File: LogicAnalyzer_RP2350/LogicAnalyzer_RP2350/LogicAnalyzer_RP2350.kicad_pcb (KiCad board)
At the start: 4 copper layers, 100 x 80 mm, 152 parts, among them J1 USB_C_Receptacle_USB2.0_16P, J2 SM03B-SRSS-TB, J3 SSW-106-02-TM-S-RA, J4 534269030, J5 534269030, J6 612050235221, J7 533984003, J8 2035571207, SW1 SW_MEC_5G, SW2 SW_MEC_5G, U1 NCP1117ST33T3G, U10 TXU0104PWR, U11 ATtiny3216-S, U2 TPS2552DRVR-1, U3 W25Q128JVS, U4 RP2350A, U5 TXU0104PWR, U6 TXU0104PWR, U7 TXU0104PWR, U8 TXU0104PWR, U9 TXU0104PWR, Y1 12Mhz

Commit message: Some PLacments
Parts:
- moved R3 6.99 mm to (133.8, 59.0), turned to 90 degrees
- moved L2 5.51 mm to (132.2, 67.3), turned to 180 degrees
- moved C3 4.51 mm to (125.9, 65.0)
- moved C2 4.35 mm to (131.3, 64.1)
- moved R33 3.93 mm to (145.0, 97.5)
- moved R34 3.93 mm to (146.0, 97.5)
- moved R35 3.93 mm to (147.0, 97.5)
- moved R14 3.42 mm to (140.7, 96.8)
- moved R4 3.18 mm to (146.5, 59.2), turned to 90 degrees
- moved R29 2.46 mm to (131.2, 97.5)
- moved R30 2.46 mm to (132.2, 97.5)
- moved R31 2.46 mm to (133.2, 97.5)
- moved R32 2.46 mm to (134.2, 97.5)
- moved C1 2.41 mm to (133.3, 64.1), turned to 90 degrees
- moved Y1 1.93 mm to (138.5, 98.1)
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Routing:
- net +3.3V: track 0.00 -> 18.1 mm, vias 0 -> 7
- net /RP2350_Main/GP12: track 0.00 -> 8.83 mm
- net /RP2350_Main/GP13: track 0.00 -> 8.46 mm
- net /RP2350_Main/GP14: track 0.00 -> 7.97 mm
- net /RP2350_Main/GP15: track 0.00 -> 7.36 mm
- net /RP2350_Main/GP18: track 0.00 -> 6.72 mm
- net /RP2350_Main/GP17: track 0.00 -> 6.53 mm
- net /RP2350_Main/GP16: track 0.00 -> 5.76 mm
- net +1V1: track 0.00 -> 4.98 mm, vias 0 -> 2
- net /RP2350_Main/XOUT: track 7.14 -> 3.23 mm
- net Net-(U2-ILIM): track 3.72 -> 0.00 mm
- net GND: track 0.00 -> 3.31 mm, vias 0 -> 6
- net Net-(U2-EN): track 2.41 -> 0.08 mm
- net Net-(U2-*FAULT): track 2.31 -> 0.00 mm
- net Net-(C13-Pad1): track 2.70 -> 4.93 mm
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
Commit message: Routing for Micro Controller Section Done
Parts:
- added C3: 4.7uF, Capacitor_SMD:C_0805_2012Metric_Pad1.18x1.45mm_HandSolder, F.Cu at (118.5, 61.0)
- C10, C11: footprint Capacitor_SMD:C_0402_1005Metric_Pad0.74x0.62mm_HandSolder -> Capacitor_0402 Small Pads for RP2350 VREG:C_0402_1005Metric_small_pads
- L3: footprint ABRACON AOTA-B201610S3R3-101-T:AOTAB201610S3R3101T -> Inductor_RP2350_Foot Print:L_pol_2016
- moved C7 8.37 mm to (109.7, 63.6)
- moved C4 8.37 mm to (98.2, 75.9)
- moved C5 8.37 mm to (109.2, 70.1)
- moved C6 8.37 mm to (107.7, 75.9)
- moved R1 8.37 mm to (99.4, 66.1)
- moved R2 8.37 mm to (99.4, 67.6)
- moved R5 8.37 mm to (105.4, 66.6)
- moved R6 8.37 mm to (105.4, 68.1)
- moved R7 8.37 mm to (105.4, 65.1)
- moved U1 8.37 mm to (102.9, 75.6)
- moved U2 8.37 mm to (109.2, 67.4)
- moved C8 5.61 mm to (120.7, 72.1)
- moved C9 5.61 mm to (119.7, 72.1)
- moved R8 5.61 mm to (120.0, 79.4)
- moved R9 5.61 mm to (120.0, 77.6)
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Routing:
- net +3.3V: track 18.1 -> 57.4 mm, vias 7 -> 21
- net GND: track 3.31 -> 39.8 mm, vias 6 -> 47
- net /LevelShifters/D1: track 0.00 -> 30.5 mm
- net /LevelShifters/D2: track 0.00 -> 29.1 mm
- net /LevelShifters/D3: track 0.00 -> 27.9 mm
- net /LevelShifters/D24: track 0.00 -> 27.1 mm
- net /LevelShifters/D4: track 0.00 -> 26.4 mm
- net /LevelShifters/D23: track 0.00 -> 26.0 mm
- net /LevelShifters/D22: track 0.00 -> 24.9 mm
- net /LevelShifters/D21: track 0.00 -> 23.5 mm
- net /LevelShifters/D5: track 0.00 -> 20.3 mm
- net /RP2350_Main/QSPI_SS: track 0.00 -> 20.0 mm
- net /LevelShifters/D9: track 0.00 -> 19.3 mm
- net /LevelShifters/D6: track 0.00 -> 19.0 mm
- net /FrontPanelInterface/VREF: track 0.00 -> 19.0 mm, vias 0 -> 6
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- added copper zone on F.Cu, net +1V1
- added copper zone on F.Cu, net +3.3V
- added copper zone on F.Cu, net GND
- added copper zone on F.Cu, net Net-(U4-VREG_LX)

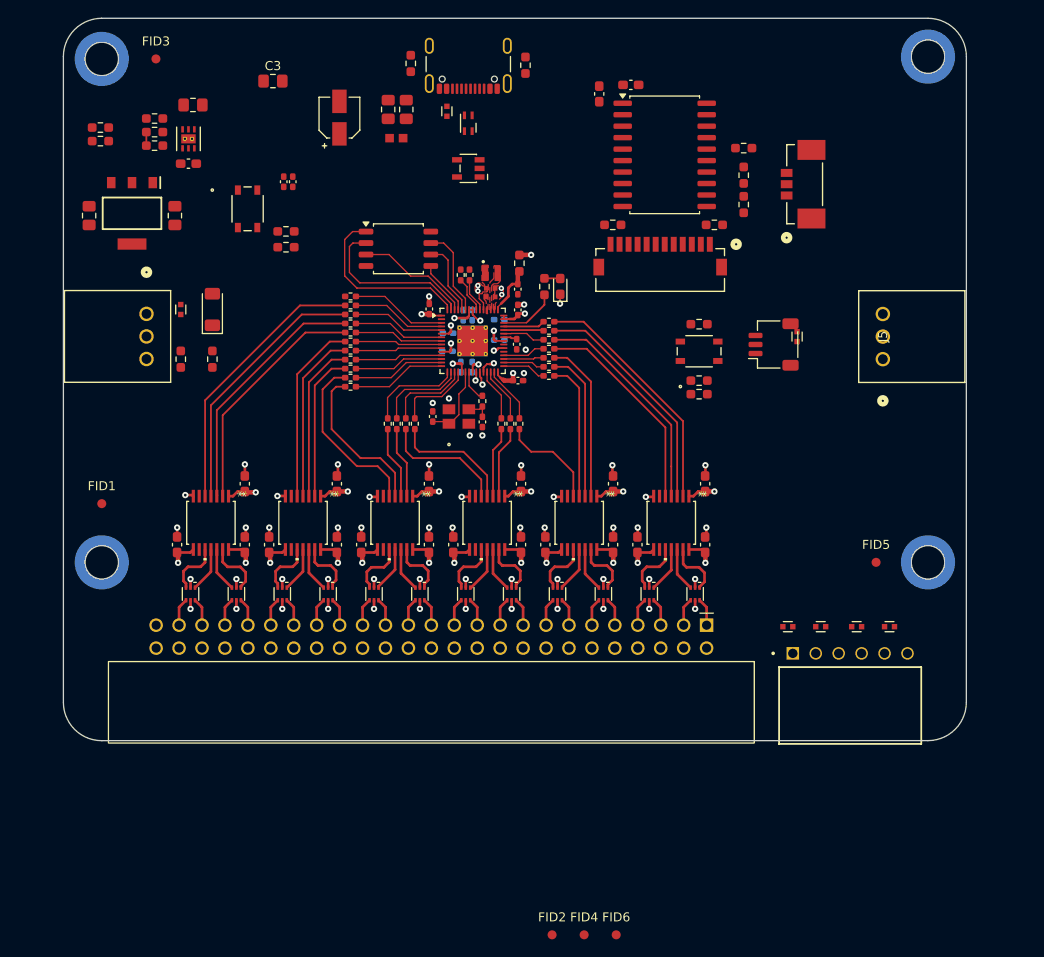
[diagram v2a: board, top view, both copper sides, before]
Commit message: Initial Routing Done, almost there
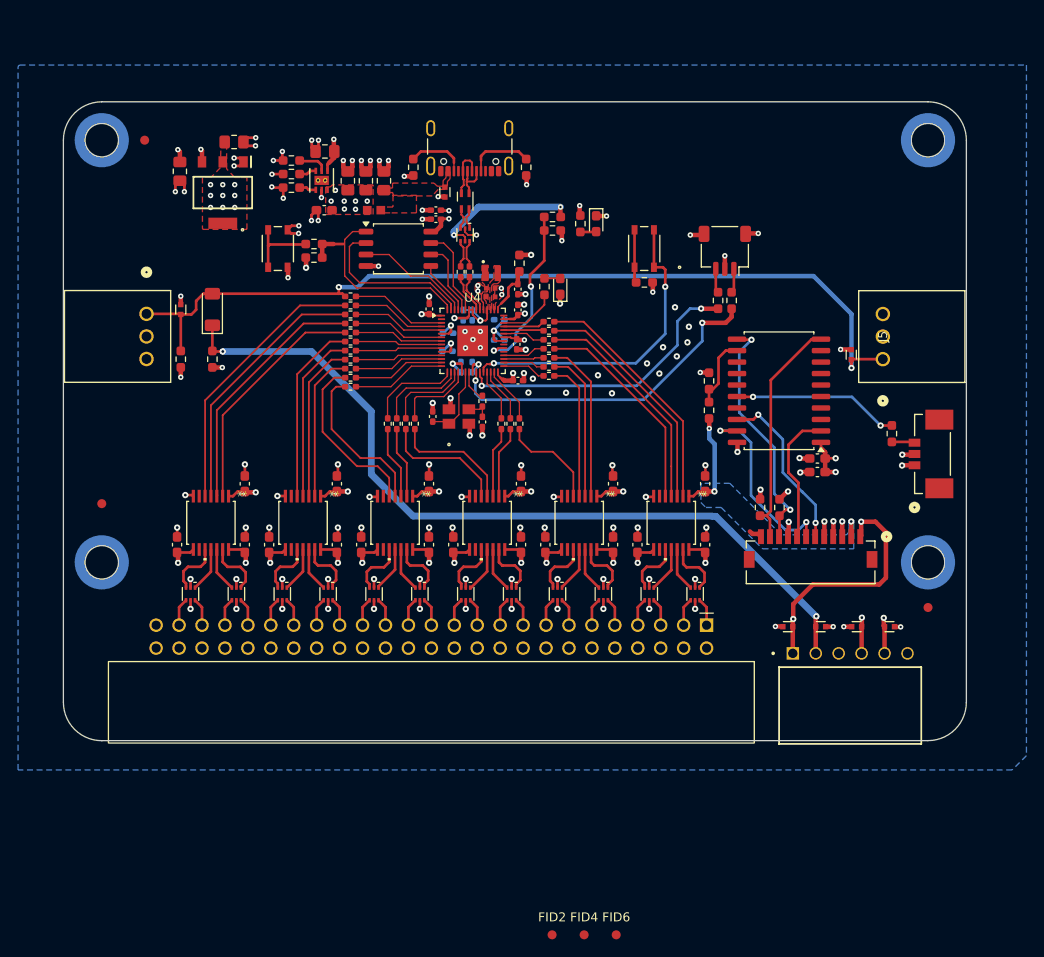
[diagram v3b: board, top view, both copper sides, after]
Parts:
- removed the C3 at (125.9, 65.0)
- added D23: LED_Blue, LED_SMD:LED_0603_1608Metric_Pad1.05x0.95mm_HandSolder, F.Cu at (154.3, 76.8)
- added R50: 470R, Resistor_SMD:R_0603_1608Metric_Pad0.98x0.95mm_HandSolder, F.Cu at (152.6, 76.8)
- D2: value SOT23-5L_824011 -> SOT563_82400152; footprint Diode_SMD_Wurth:D_Wurth_WE-TVS-SOT23-5L -> Diode_SMD_Wurth:D_Wurth_WE-TVS-SOT563
- U4: footprint Package_DFN_QFN:QFN-60-1EP_7x7mm_P0.4mm_EP3.4x3.4mm_ThermalVias -> Package_DFN_QFN:QFN-60-1EP_7x7mm_P0.4mm_EP3.4x3.4mm
- moved R1 51.0 mm to (149.5, 76.0)
- moved R2 51.0 mm to (149.5, 77.5)
- moved C46 48.3 mm to (178.8, 104.3), turned to 180 degrees
- moved C45 46.2 mm to (178.8, 102.8), turned to 180 degrees
- moved J8 36.4 mm to (178.1, 114.3)
- moved R47 35.6 mm to (187.1, 100.0), turned to 90 degrees
- moved R49 35.3 mm to (172.5, 108.2), turned to 90 degrees
- moved J7 33.1 mm to (191.6, 102.3)
- moved R48 32.1 mm to (174.6, 108.2), turned to 90 degrees
- moved U11 29.0 mm to (174.6, 95.3), turned to 180 degrees
- moved R45 26.3 mm to (166.8, 97.4), turned to -90 degrees
- moved R46 19.9 mm to (166.8, 94.2), turned to -90 degrees
- moved C9 17.1 mm to (136.6, 75.3), turned to 180 degrees
- moved C8 16.4 mm to (136.6, 76.3), turned to 180 degrees
- moved C5 15.9 mm to (124.2, 75.3)
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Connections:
- D2 pad 1: unconnected-(D2-NC-Pad1) -> /USB & POWER/TUSBC-
- D2 pad 3: /RP2350_Main/USB+ -> /USB & POWER/TUSBC+
- D2 pad 4: /RP2350_Main/USB- -> /RP2350_Main/USB+
- L1 pad 1: /USB & POWER/USBC+ -> /USB & POWER/TUSBC+
- L1 pad 2: /RP2350_Main/USB+ -> /USB & POWER/USBC+
- L1 pad 3: /RP2350_Main/USB- -> /USB & POWER/USBC-
- L1 pad 4: /USB & POWER/USBC- -> /USB & POWER/TUSBC-
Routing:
- net /LevelShifters/EXT_CHAIN: track 0.00 -> 97.9 mm, vias 0 -> 2
- net /LevelShifters/EXT_TRIG: track 0.00 -> 90.1 mm, vias 0 -> 2
- net GND: track 39.8 -> 110.0 mm, vias 47 -> 115
- net +3.3V: track 57.4 -> 93.9 mm, vias 21 -> 40
- net /RP2350_Main/SWCLK: track 1.01 -> 37.0 mm, vias 1 -> 2
- net Net-(U4-RUN): track 1.84 -> 34.8 mm, vias 1 -> 2
- net +5V: track 11.4 -> 43.4 mm, vias 12 -> 20
- net /RP2350_Main/SWDIO: track 1.85 -> 33.1 mm, vias 1 -> 2
- net Net-(U11-PB0): track 0.00 -> 27.2 mm, vias 0 -> 2
- net /FrontPanelInterface/EXTVREF: track 0.00 -> 26.9 mm, vias 0 -> 2
- net Net-(U11-PB1): track 0.00 -> 26.5 mm
- net /FrontPanelInterface/LEDB: track 0.00 -> 21.4 mm, vias 0 -> 2
- net /FrontPanelInterface/LEDA: track 0.00 -> 18.8 mm, vias 0 -> 2
- net Net-(U11-~{RESET}/PA0): track 0.00 -> 18.5 mm, vias 0 -> 2
- net /RP2350_Main/VBUS_SENSE: track 1.22 -> 19.3 mm, vias 1 -> 2
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- added copper zone on In2.Cu, net +1V1
- added copper zone on In2.Cu, net +3.3V
- added copper zone on In2.Cu, net +5V
- added copper zone on B.Cu, net /FrontPanelInterface/VREF
- added copper zone on In2.Cu, net /FrontPanelInterface/VREF
- added copper zone on F.Cu, net /USB & POWER/VBUS
- added copper zone on F.Cu, net /USB & POWER/VBUS_FILT
- added copper zone on In2.Cu, net /USB & POWER/VBUS_FILT
- added copper zone on B.Cu, net GND
- added copper zone on In1.Cu, net GND
- added copper zone on In2.Cu, net GND
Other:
- board size 100 x 80 mm -> 100 x 70.7 mm

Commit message: more routing
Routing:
- net /RP2350_Main/VBUS_SENSE: track 19.3 -> 26.1 mm
- net +3.3V: track 93.9 -> 90.8 mm
- net Net-(U11-PB1): track 26.5 -> 29.1 mm
- net /FrontPanelInterface/EXTVREF: track 26.9 -> 28.9 mm, vias 2 -> 0
- net GND: track 110.0 -> 109.3 mm, vias 115 -> 107
- added copper zone on B.Cu, net +3.3V
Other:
- rule pad_to_mask_clearance: 0.1 -> 0.035
- rule solder_mask_min_width: 0.1 -> 0.035

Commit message: Almost there
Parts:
- added REF**: KiCad-Logo2_5mm_SilkScreen, Symbol:KiCad-Logo2_5mm_SilkScreen, F.Cu at (103.7, 101.1)
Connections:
- net /RP2350_Main/USB_BOOT renamed /RP2350_Main/RP_BOOT
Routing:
- net GND: track 109.3 -> 107.8 mm, vias 107 -> 106

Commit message: Correcting Diff pair USB
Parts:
- moved D2 3.97 mm to (140.8, 74.2)
- moved L1 3.54 mm to (140.8, 77.7)
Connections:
- D2 pad 1: /USB & POWER/TUSBC- -> /USB & POWER/USBC-
- D2 pad 3: /USB & POWER/TUSBC+ -> /USB & POWER/USBC+
- D2 pad 4: /RP2350_Main/USB+ -> /USB & POWER/TUSBC+
- D2 pad 6: /RP2350_Main/USB- -> /USB & POWER/TUSBC-
- L1 pad 1: /USB & POWER/TUSBC+ -> /RP2350_Main/USB+
- L1 pad 2: /USB & POWER/USBC+ -> /USB & POWER/TUSBC+
- L1 pad 3: /USB & POWER/USBC- -> /USB & POWER/TUSBC-
- L1 pad 4: /USB & POWER/TUSBC- -> /RP2350_Main/USB-
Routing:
- net +5V: track 43.4 -> 30.0 mm
- net GND: track 107.8 -> 104.5 mm, vias 106 -> 104
- net /USB & POWER/USBC+: track 5.68 -> 4.54 mm
- net /USB & POWER/USBC-: track 4.67 -> 5.72 mm
- net /RP2350_Main/USB-: track 3.06 -> 3.61 mm

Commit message: filleting the tracks
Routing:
- net +3.3V: track 90.8 -> 94.1 mm
